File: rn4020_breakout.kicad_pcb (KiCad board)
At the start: 2 copper layers, 62.2 x 22.9 mm, 2 parts, among them P1 CONN_01X22, U1 RN4020

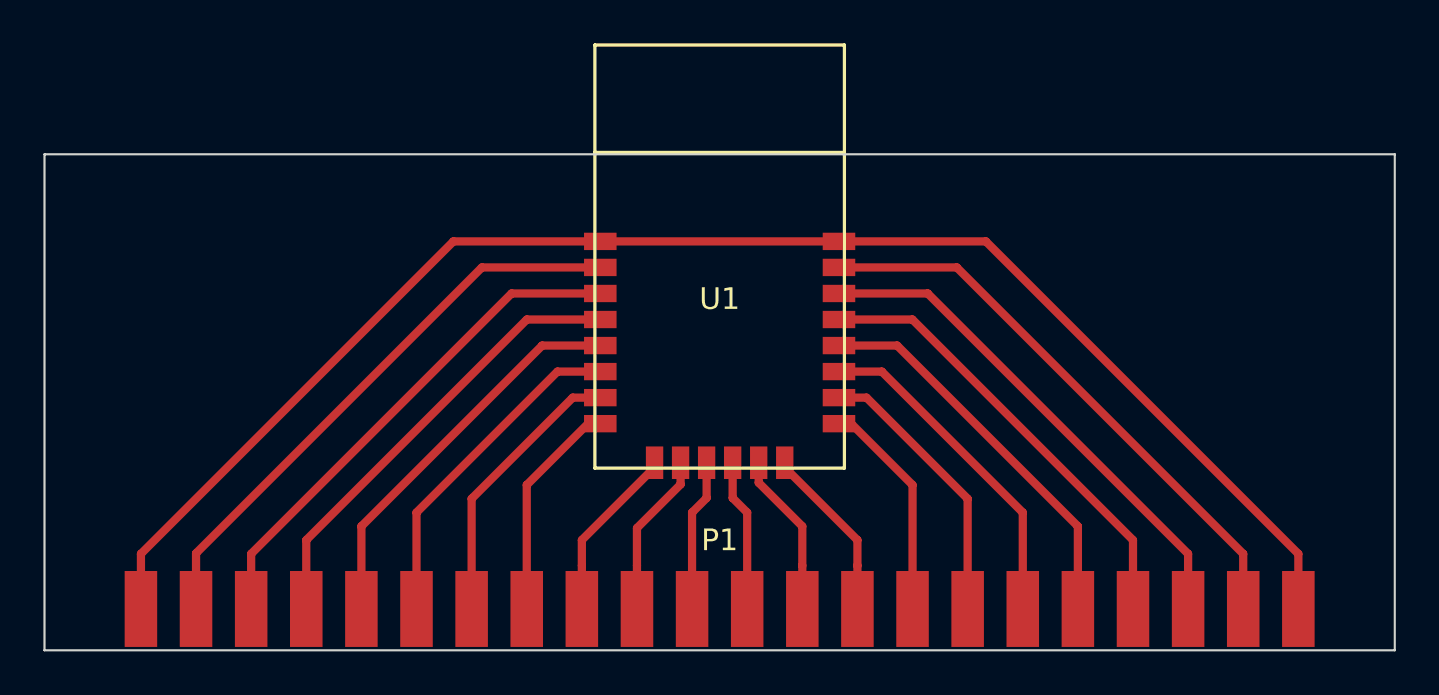
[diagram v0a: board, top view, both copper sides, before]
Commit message: Fix bad RN4020 footprint
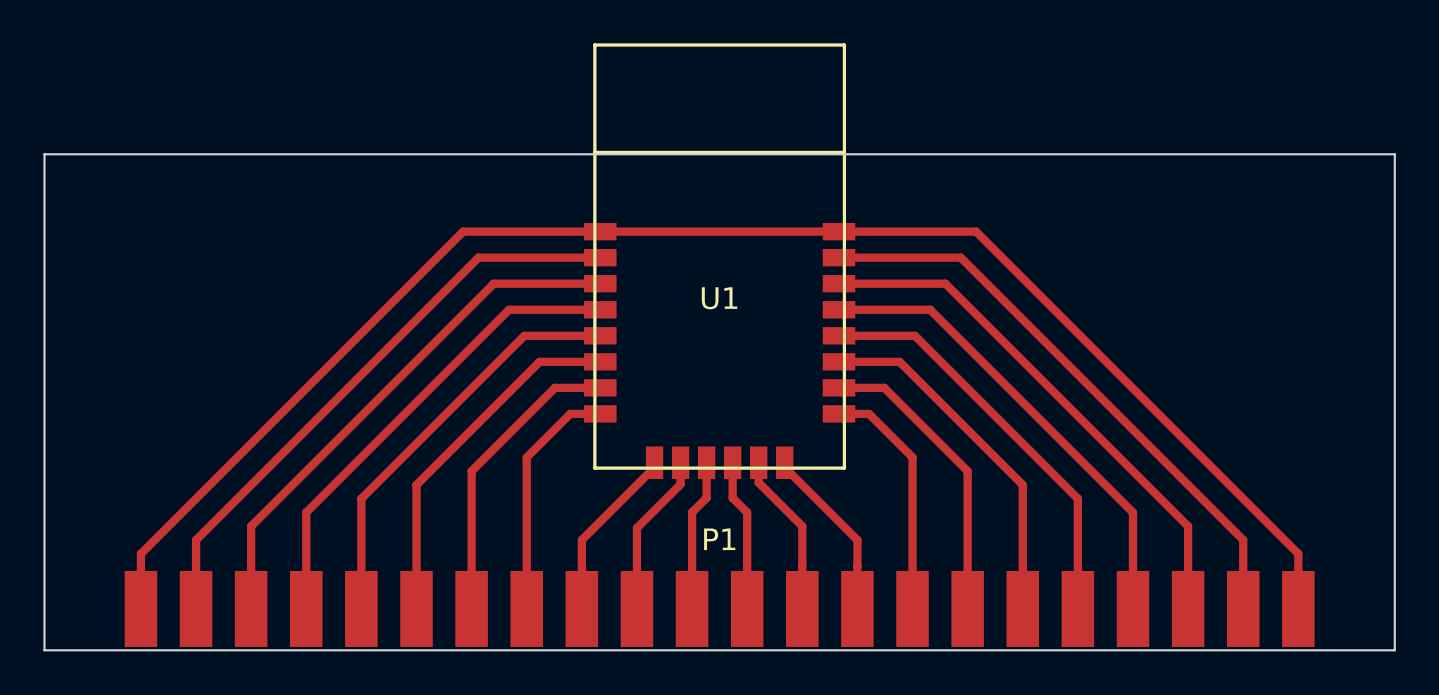
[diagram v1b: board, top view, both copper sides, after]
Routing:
- net Net-(P1-Pad19): track 21.9 -> 22.9 mm
- net Net-(P1-Pad7): track 12.9 -> 13.9 mm
- net Net-(P1-Pad17): track 15.6 -> 16.5 mm
- net Net-(P1-Pad4): track 21.9 -> 22.9 mm
- net Net-(P1-Pad5): track 19.9 -> 20.8 mm
- net Net-(P1-Pad18): track 19.9 -> 20.8 mm
- net Net-(P1-Pad16): track 13.9 -> 14.9 mm
- net Net-(P1-Pad6): track 15.6 -> 16.5 mm
- net Net-(P1-Pad3): track 24.6 -> 25.5 mm
- net Net-(P1-Pad20): track 24.6 -> 25.5 mm
- net Net-(P1-Pad8): track 10.6 -> 11.2 mm
- net Net-(P1-Pad15): track 10.6 -> 11.2 mm
- net Net-(P1-Pad21): track 27.6 -> 28.2 mm
- net Net-(P1-Pad2): track 27.7 -> 28.2 mm
